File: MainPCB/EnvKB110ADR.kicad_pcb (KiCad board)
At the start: 2 copper layers, 429.5 x 125 mm, 245 parts, among them SW1 Boot Mode, SW2 Reset Switch, U1 XC6206PxxxMR, U2 STM32F411CEUx, X1 ECS-2520MV-xxx-xx

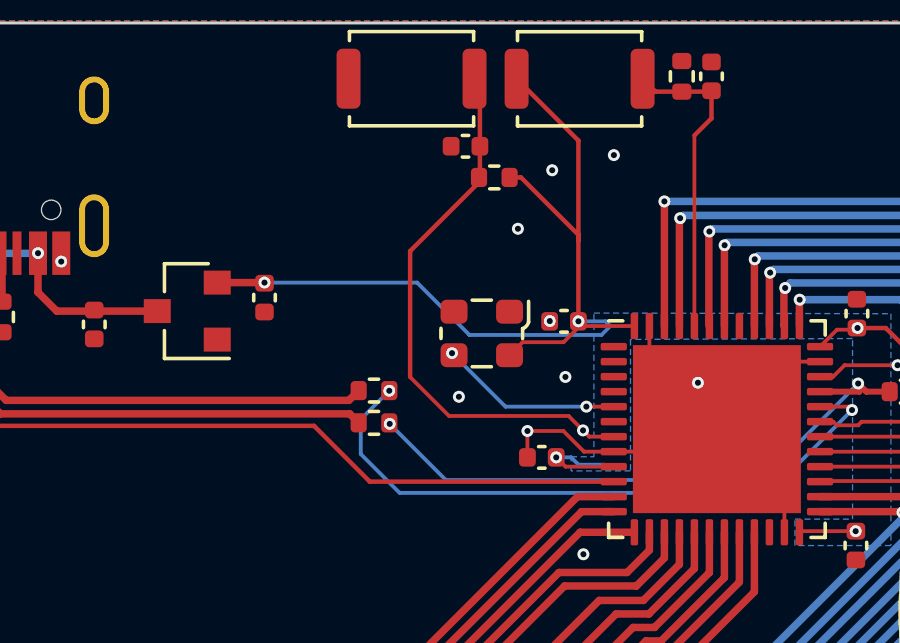
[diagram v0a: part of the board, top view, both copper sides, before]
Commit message: changed oscillator for crystal, re-added libraries, made change in PCBNew
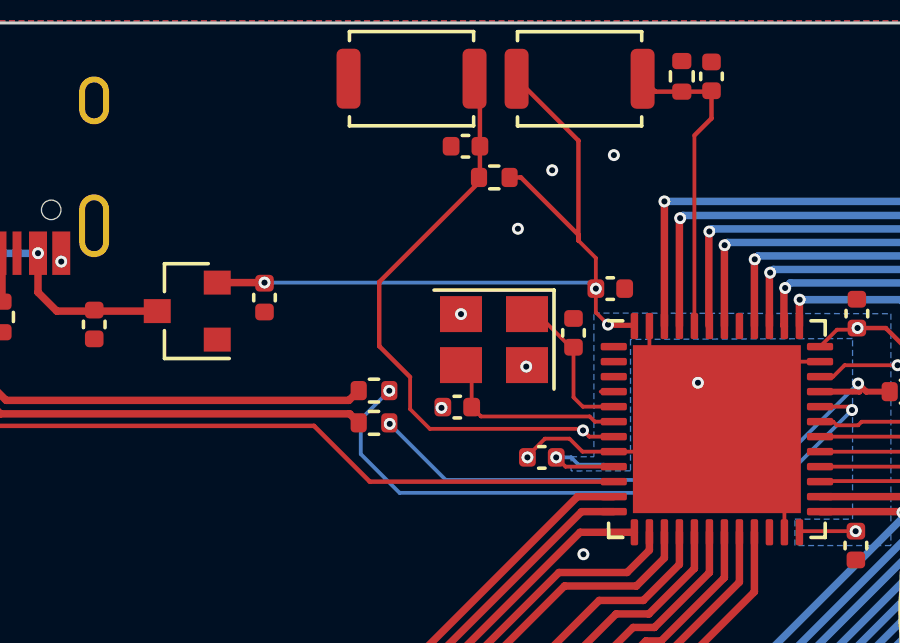
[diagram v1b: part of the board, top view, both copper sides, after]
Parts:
- removed X1: ECS-2520MV-xxx-xx, Oscillator:Oscillator_SMD_ECS_2520MV-xxx-xx-4Pin_2.5x2.0mm
- added C10: 0402 22pF, Capacitor_SMD:C_0402_1005Metric, F.Cu at (408.9, 64.3)
- added C9: 0402 22pF, Capacitor_SMD:C_0402_1005Metric, F.Cu at (412.8, 61.9)
- added Y1: 3225_4P 32.768khz, Crystal:Crystal_SMD_3225-4Pin_3.2x2.5mm, F.Cu at (410.1, 62.1)
- moved C1 1.89 mm to (414.0, 60.4), turned to 0 degrees
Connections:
- U2 pad 5: OSCpin -> Net-(C9-Pad1)
- USB1 pad 13: GND -> Net-(USB1-Pad13)
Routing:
- net Net-(C10-Pad1): track 0.00 -> 6.49 mm
- net OSCpin: track 6.13 -> 0.00 mm, vias 2 -> 0
- net Net-(C9-Pad1): track 0.00 -> 5.15 mm
- net +3V3: track 42.8 -> 38.0 mm, vias 5 -> 6
- net resetsw: track 18.6 -> 20.0 mm
- net GND: track 22.4 -> 21.7 mm

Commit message: Small fixes and corrections
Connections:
- USB1 pad 13: Net-(USB1-Pad13) -> GND

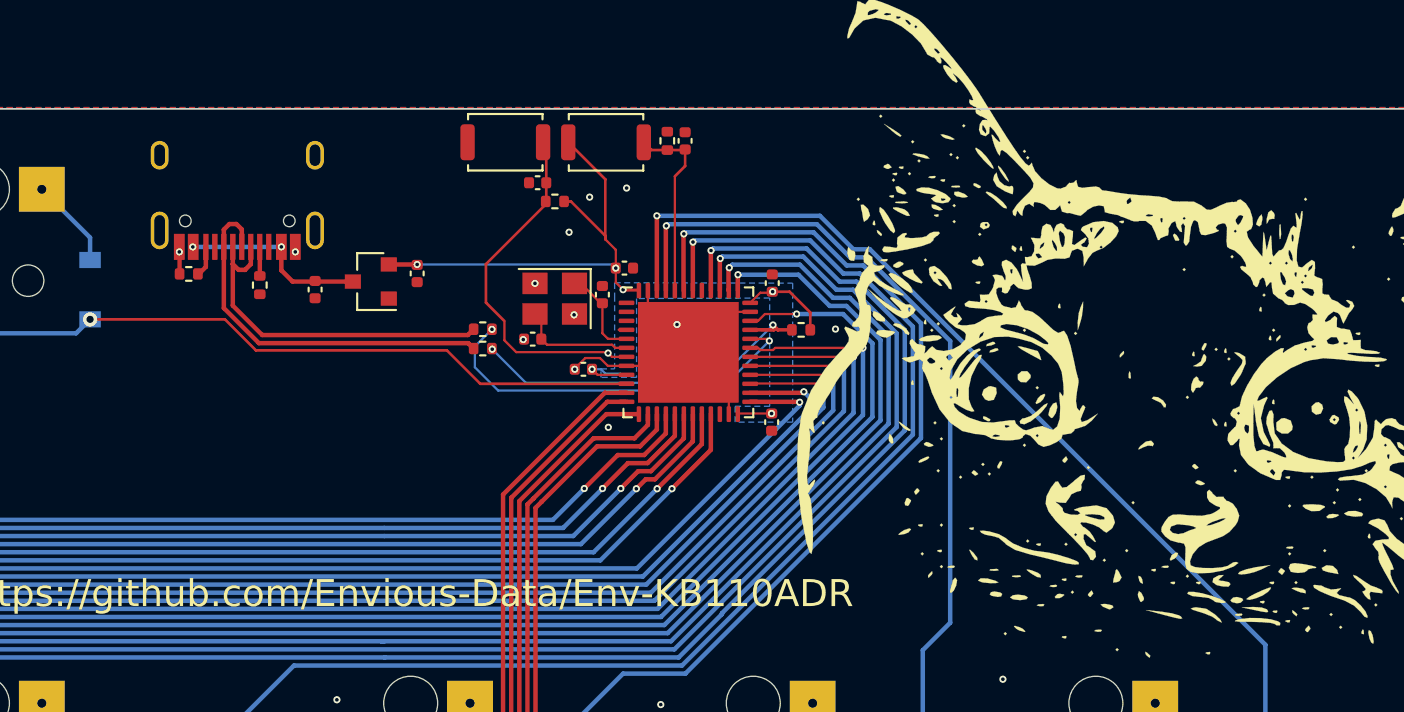
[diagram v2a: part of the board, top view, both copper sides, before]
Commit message: some general changes, might change MCU to RP2040
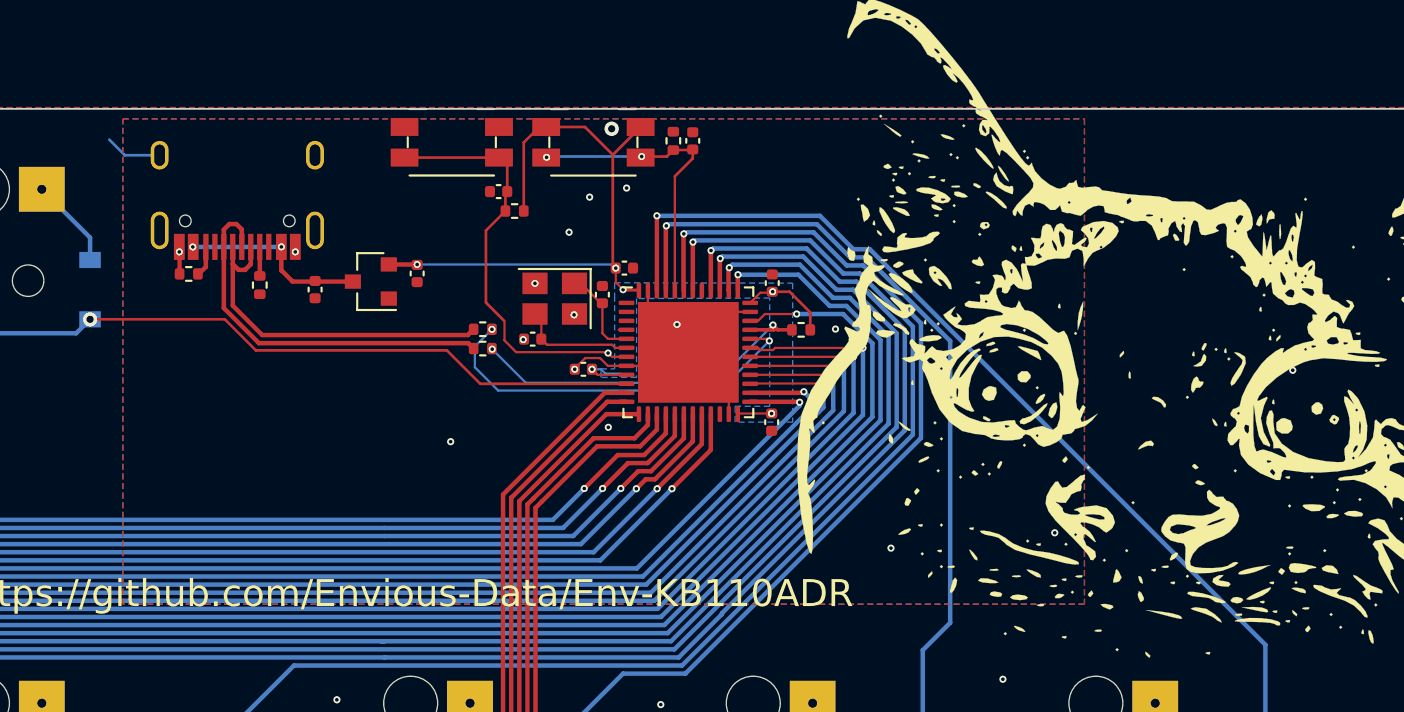
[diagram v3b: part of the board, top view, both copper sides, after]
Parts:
- SW1, SW2: footprint Button_Switch_SMD:SW_Push_SPST_NO_Alps_SKRK -> Button_Switch_SMD:Panasonic_EVQPUJ_EVQPUA
- moved SW2 2.98 mm to (404.4, 53.4)
- moved R7 2.30 mm to (407.9, 57.2)
- moved C8 2.23 mm to (407.0, 56.1)
- moved SW1 0.70 mm to (412.2, 53.4)
- moved C7 0.42 mm to (417.8, 53.3)
- moved R6 0.33 mm to (416.7, 53.3)
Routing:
- net +3V3: track 38.0 -> 45.0 mm
- net boot0: track 10.5 -> 16.4 mm, vias 0 -> 2
- net resetsw: track 20.0 -> 23.7 mm
- net GND: track 21.7 -> 24.9 mm, vias 39 -> 44

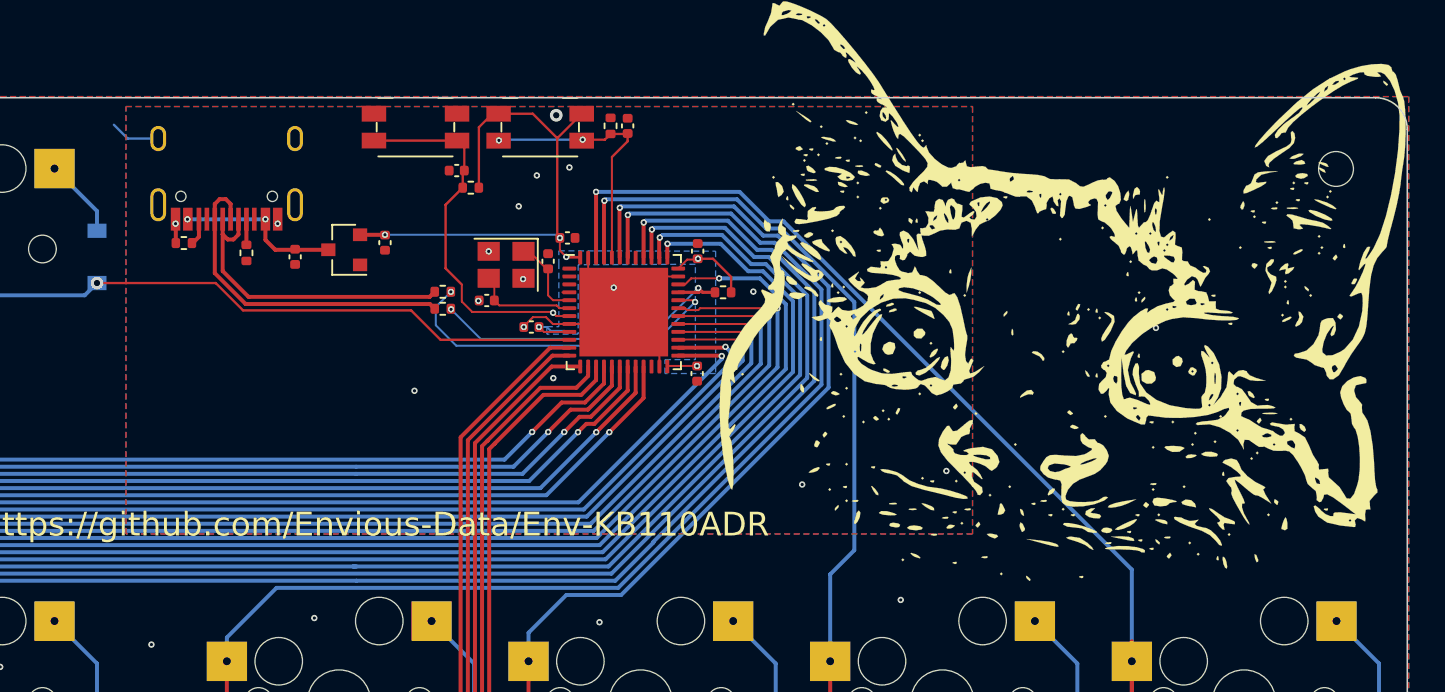
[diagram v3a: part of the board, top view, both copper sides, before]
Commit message: Converted board from STM32F411CEU6 to RP2040
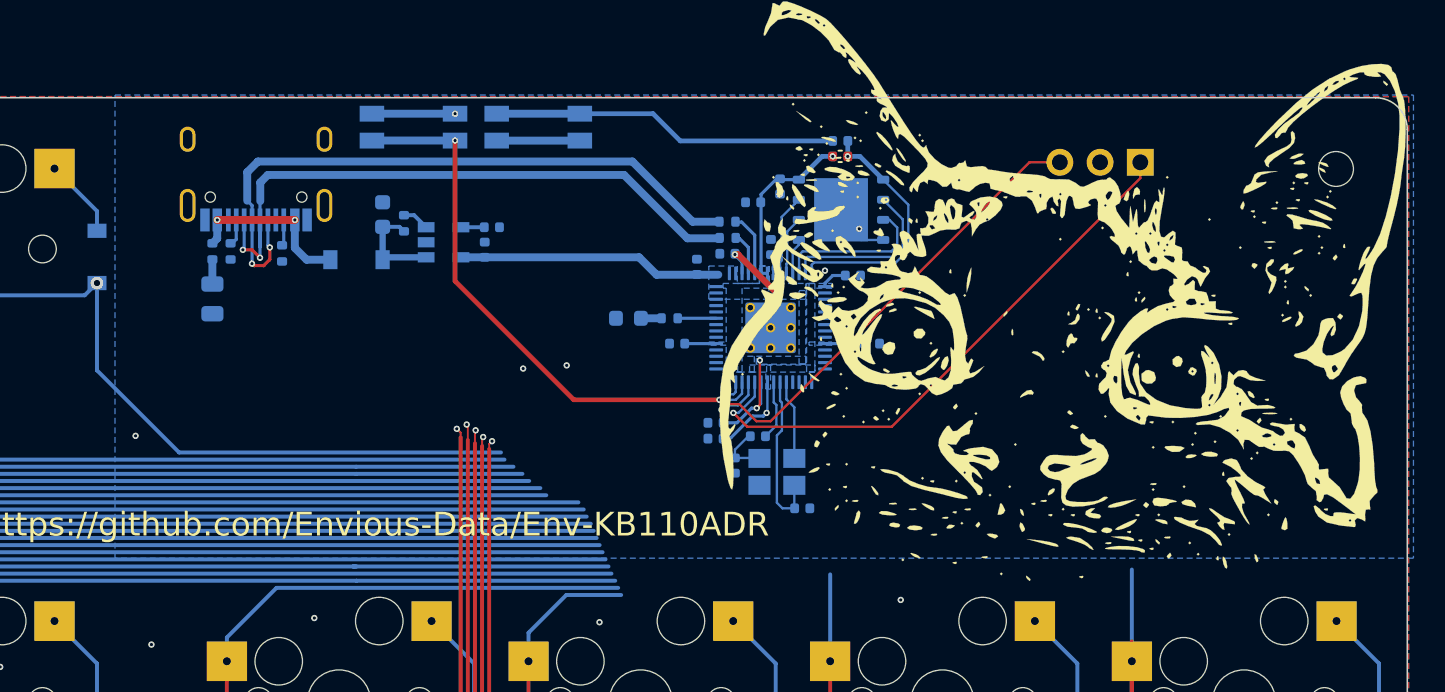
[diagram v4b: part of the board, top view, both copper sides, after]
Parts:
- removed C8: 100nf 0402, Capacitor_SMD:C_0402_1005Metric
- removed C9: 0402 22pF, Capacitor_SMD:C_0402_1005Metric
- removed SW1: Boot Mode, Button_Switch_SMD:Panasonic_EVQPUJ_EVQPUA
- removed SW2: Reset Switch, Button_Switch_SMD:Panasonic_EVQPUJ_EVQPUA
- removed U2: STM32F411CEUx, Package_DFN_QFN:QFN-48-1EP_7x7mm_P0.5mm_EP5.6x5.6mm
- added C11: 100nf 0402, Capacitor_SMD:C_0402_1005Metric, B.Cu at (425.7, 58.1)
- added C14: 100nf 0402, Capacitor_SMD:C_0402_1005Metric, B.Cu at (433.2, 67.0)
- added C15: 100nf 0402, Capacitor_SMD:C_0402_1005Metric, B.Cu at (432.0, 62.8)
- added C16: 100nf 0402, Capacitor_SMD:C_0402_1005Metric, B.Cu at (423.3, 73.0)
- added C18: 100nf 0402, Capacitor_SMD:C_0402_1005Metric, B.Cu at (420.9, 67.0)
- added C19: 22pf 0402, Capacitor_SMD:C_0402_1005Metric, B.Cu at (424.6, 74.8)
- added CBP1: 10uf 0402, Capacitor_SMD:C_0402_1005Metric, B.Cu at (409.2, 59.7)
- added D1: 1N4002W, Diode_SMD:D_SOD-123, B.Cu at (400.6, 61.8)
- added D3: LED_0603, LED_SMD:LED_0603_1608Metric, B.Cu at (417.8, 65.5)
- added FLASH1: W25Q128JVPIQ, Package_SON:WSON-8-1EP_6x5mm_P1.27mm_EP3.4x4mm, B.Cu at (431.2, 58.6)
- added J2: EVQPU, Button_Switch_SMD:Panasonic_EVQPUJ_EVQPUA, B.Cu at (412.1, 53.4)
- added J5: Conn_01x03_Male, Connector_PinHeader_2.54mm:PinHeader_1x03_P2.54mm_Horizontal, B.Cu at (450.1, 55.6)
- added PWRLED1: LED_0603, LED_SMD:LED_0805_2012Metric, B.Cu at (391.6, 64.2)
- added R11: 1K 0402 Resistor, Capacitor_SMD:C_0402_1005Metric, B.Cu at (426.0, 72.9)
- added R12: 1K 0402 Resistor, Resistor_SMD:R_0402_1005Metric, B.Cu at (391.6, 61.2)
- added R8: 470 0402 Resistor, Resistor_SMD:R_0402_1005Metric, B.Cu at (420.4, 65.5)
- added RSW1: EVQPU, Button_Switch_SMD:Panasonic_EVQPUJ_EVQPUA, B.Cu at (404.2, 53.4)
- added U3: RP2040, RP2040_minimal:RP2040-QFN-56, B.Cu at (426.8, 66.0)
- C1: value 100nf capacitor -> 10uf 0603 6.3V; footprint Capacitor_SMD:C_0402_1005Metric -> Capacitor_SMD:C_0603_1608Metric; moved to B.Cu
- C10: value 0402 22pF -> 1uf 0402; moved to B.Cu
- C2: value 100nf capacitor -> 22pf 0402; moved to B.Cu
- C3: value 100nf capacitor -> 1uf 0402; moved to B.Cu
- C4: value 100nf capacitor -> 10uf 0402; moved to B.Cu
- C5, C6: value 1uf capacitor -> 100nf 0402; moved to B.Cu
- C7, R5: moved to B.Cu
- R1: value 1.5K 0402 -> 1K 0402 Resistor; footprint Resistor_SMD:R_0402_1005Metric -> Capacitor_SMD:C_0402_1005Metric; moved to B.Cu
- R2: value 5.1K 0402 -> DNF; footprint Resistor_SMD:R_0402_1005Metric -> Capacitor_SMD:C_0402_1005Metric
- R3, R4: value 22ohm -> 27 0402 Resistor; moved to B.Cu
- R6: value 100k 0402 -> 5.1K 0402; moved to B.Cu
- R7: value 10K 0402 -> 100K 0402 resistor; moved to B.Cu
- U1: value XC6206PxxxMR -> TLV75533PDBVR; footprint Package_TO_SOT_SMD:SOT-23 -> Package_TO_SOT_SMD:SOT-23-5; moved to B.Cu
- USB1: value HRO-TYPE-C-31-M-12 -> TYPE-C-31-M-12; footprint Type-C:HRO-TYPE-C-31-M-12-Assembly -> HRO-TYPE-C31-M-12:HRO-TYPE-C-31-M-12; moved to B.Cu
- Y1: value 3225_4P 32.768khz -> 3225_4P; moved to B.Cu
- moved R2 38.0 mm to (431.2, 55.2), turned to 0 degrees
- moved C5 30.9 mm to (427.4, 57.1), turned to 270 degrees
- moved C6 23.8 mm to (423.3, 72.0), turned to 180 degrees
- moved R6 22.3 mm to (395.9, 61.4)
- moved Y1 21.5 mm to (427.2, 75.2)
- moved R3 18.8 mm to (424.1, 59.4), turned to 0 degrees
- moved R4 18.3 mm to (424.1, 60.4), turned to 0 degrees
- moved C2 17.5 mm to (428.8, 77.5), turned to 180 degrees
- moved C4 15.5 mm to (408.8, 61.1)
- moved C10 13.4 mm to (422.1, 62.2), turned to 90 degrees
- moved C3 13.2 mm to (424.1, 61.4), turned to 180 degrees
- moved R1 12.1 mm to (431.2, 54.2)
- moved C7 11.9 mm to (426.8, 61.0)
- moved C1 11.8 mm to (402.3, 58.9), turned to 90 degrees
- moved U1 6.29 mm to (406.1, 60.6), turned to 0 degrees
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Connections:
- C1 pad 1: +3V3 -> VSYS
- C10 pad 1: Net-(C10-Pad1) -> +3V3
- C2 pad 2: +3V3 -> XIN
- C3 pad 1: GND -> +1V1
- C3 pad 2: +3V3 -> GND
- C4 pad 1: GND -> +3V3
- C4 pad 2: +3V3 -> GND
- C5 pad 1: GND -> +3V3
- C5 pad 2: VBUS -> GND
- C6 pad 1: GND -> +1V1
- C6 pad 2: +3V3 -> GND
- C7 pad 1: boot0 -> +1V1
- R1 pad 1: +3V3 -> /QSPI_SS
- R1 pad 2: PA12 -> /~USB_BOOT
- R2 pad 1: GND -> +3V3
- R2 pad 2: Net-(R2-Pad2) -> /QSPI_SS
- R3 pad 1: PA12 -> USB_D+
- R3 pad 2: D+ -> Net-(R3-Pad2)
- R4 pad 1: PA11 -> USB_D-
- R4 pad 2: D- -> Net-(R4-Pad2)
- R6 pad 1: boot0 -> GND
- R6 pad 2: GND -> Net-(R6-Pad2)
- R7 pad 1: resetsw -> 3V3_EN
- R7 pad 2: +3V3 -> VSYS
- U1 pad 1: GND -> VSYS
- U1 pad 2: +3V3 -> GND
- U1 pad 3: VBUS -> 3V3_EN
- USB1 pad 10: Net-(R5-Pad2) -> Net-(R6-Pad2)
- USB1 pad 4: Net-(R2-Pad2) -> Net-(R5-Pad2)
- USB1 pad 5: D- -> USB_D-
- USB1 pad 6: D+ -> USB_D+
- USB1 pad 7: D- -> USB_D-
- USB1 pad 8: D+ -> USB_D+
- Y1 pad 1: Net-(C9-Pad1) -> XIN
- Y1 pad 3: Net-(C10-Pad1) -> Net-(C19-Pad2)
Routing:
- net col22: track 167.7 -> 119.8 mm, vias 1 -> 0
- net col20: track 109.2 -> 65.8 mm, vias 1 -> 0
- net USB_D+: track 0.00 -> 43.3 mm, vias 0 -> 2
- net USB_D-: track 0.00 -> 41.7 mm, vias 0 -> 2
- net col19: track 148.8 -> 107.7 mm, vias 1 -> 0
- net col21: track 123.1 -> 83.2 mm, vias 1 -> 0
- net col17: track 194.2 -> 155.9 mm, vias 1 -> 0
- net /RUN: track 0.00 -> 36.3 mm, vias 0 -> 2
- net /SWCLK: track 0.00 -> 36.2 mm, vias 0 -> 1
- net col16: track 211.2 -> 175.1 mm, vias 1 -> 0
- net col15: track 227.6 -> 193.8 mm, vias 1 -> 0
- net /SWD: track 0.00 -> 31.6 mm, vias 0 -> 1
- net col14: track 273.1 -> 241.6 mm, vias 1 -> 0
- net col12: track 251.1 -> 223.0 mm, vias 1 -> 0
- net col11: track 311.1 -> 285.1 mm, vias 1 -> 0
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- added copper zone on B.Cu, net +1V1

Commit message: wired up all the traces required to make the keyboard functional.
However this means you can no longer use the Rpi pico firmware with this and needs a custom compiled firmware to utilize the normally unavailable pins,
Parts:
- PWRLED1: value LED_0603 -> LED_0805
- moved R8 2.68 mm to (417.8, 65.5)
- moved D3 2.60 mm to (415.2, 65.5)
- moved C18 0.61 mm to (420.3, 67.2)
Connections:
- U3 pad 11: /GPIO8 -> col14
- U3 pad 12: /GPIO9 -> col12
- U3 pad 13: /GPIO10 -> col11
- U3 pad 14: /GPIO11 -> col10
- U3 pad 15: /GPIO12 -> col9
- U3 pad 16: /GPIO13 -> col8
- U3 pad 17: /GPIO14 -> col7
- U3 pad 18: /GPIO15 -> col6
- U3 pad 27: /GPIO16 -> col5
- U3 pad 28: /GPIO17 -> col4
- U3 pad 29: /GPIO18 -> col3
- U3 pad 3: /GPIO1 -> col22
- U3 pad 30: /GPIO19 -> col2
- U3 pad 31: /GPIO20 -> col1
- U3 pad 32: /GPIO21 -> col0
- U3 pad 34: /GPIO22 -> col13
- U3 pad 35: /GPIO23 -> row7
- U3 pad 36: /GPIO24 -> row6
- U3 pad 38: /GPIO26_ADC0 -> row5
- U3 pad 39: /GPIO27_ADC1 -> row4
- U3 pad 4: /GPIO2 -> col21
- U3 pad 40: /GPIO28_ADC2 -> row3
- U3 pad 41: /GPIO29_ADC3 -> row1
- U3 pad 5: /GPIO3 -> col20
- U3 pad 6: /GPIO4 -> col19
- U3 pad 7: /GPIO5 -> col17
- U3 pad 8: /GPIO6 -> col16
- U3 pad 9: /GPIO7 -> col15
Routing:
- net col20: track 65.8 -> 104.0 mm
- net col19: track 107.7 -> 145.1 mm
- net col17: track 155.9 -> 192.3 mm
- net col16: track 175.1 -> 210.6 mm
- net col15: track 193.8 -> 228.4 mm
- net col22: track 119.8 -> 149.8 mm
- net col14: track 241.6 -> 271.4 mm
- net col12: track 223.0 -> 251.6 mm
- net col11: track 285.1 -> 313.0 mm
- net col10: track 308.1 -> 334.8 mm
- net col9: track 307.1 -> 332.6 mm
- net col8: track 326.1 -> 351.4 mm
- net col7: track 345.1 -> 370.1 mm
- net col6: track 351.7 -> 376.4 mm
- net col21: track 83.2 -> 107.5 mm
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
